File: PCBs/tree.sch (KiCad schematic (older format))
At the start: 1 part

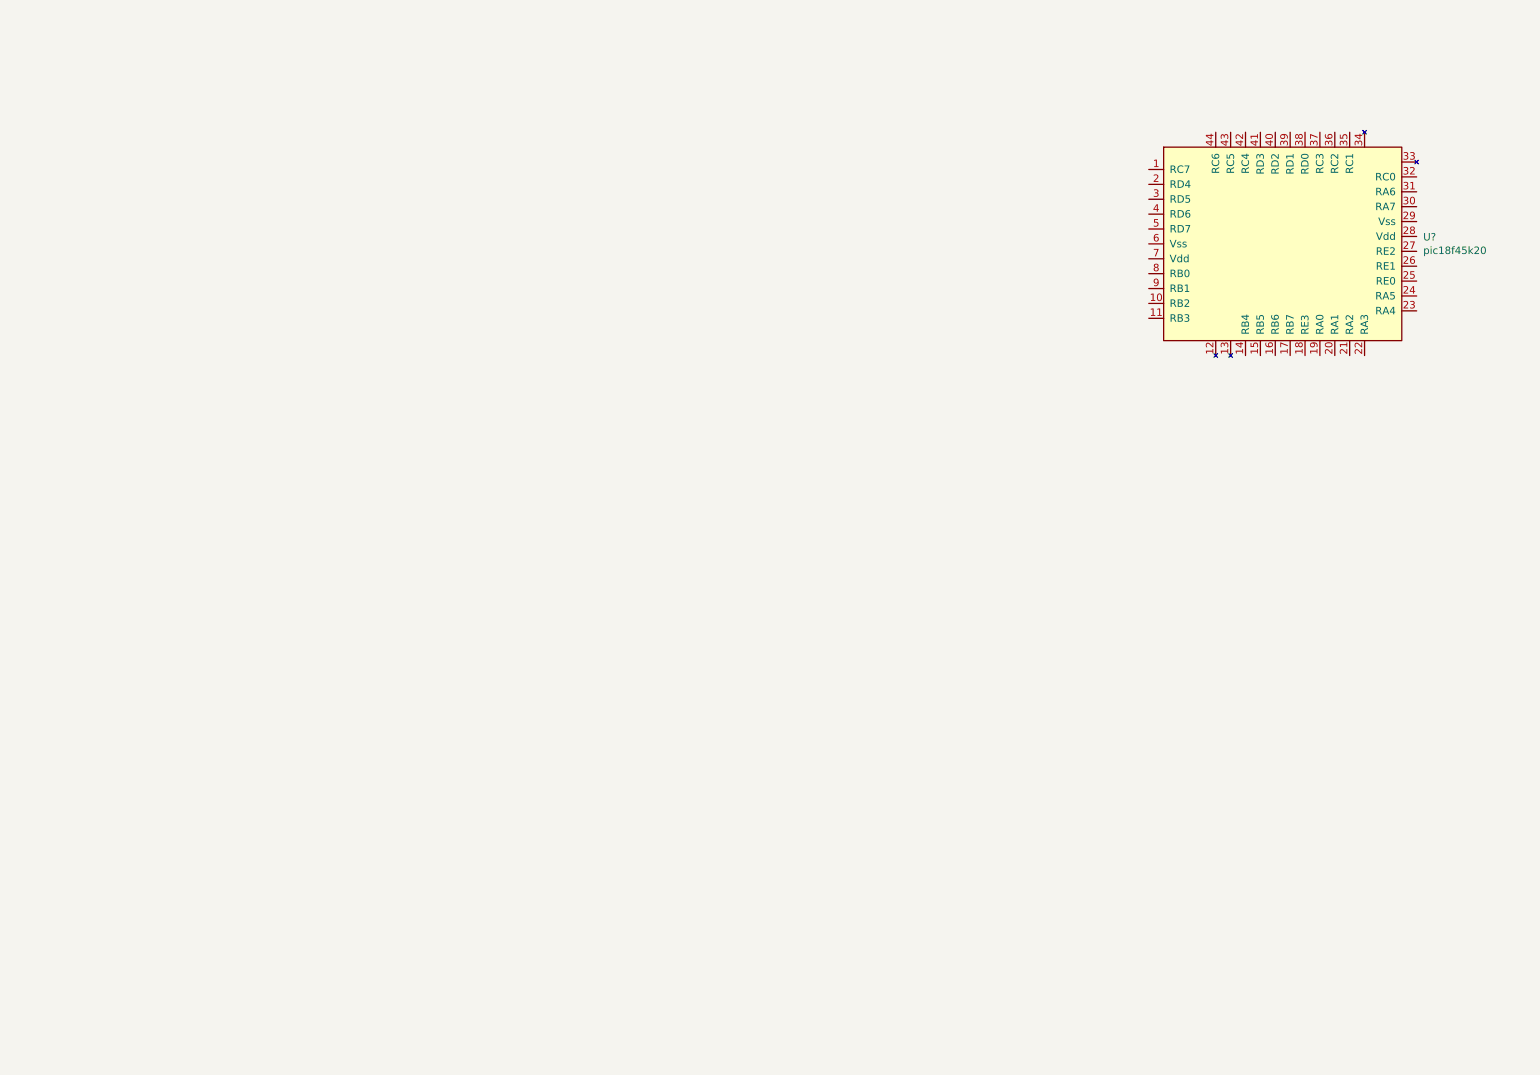
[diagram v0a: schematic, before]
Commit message: Pre-Shift Reg Schematic
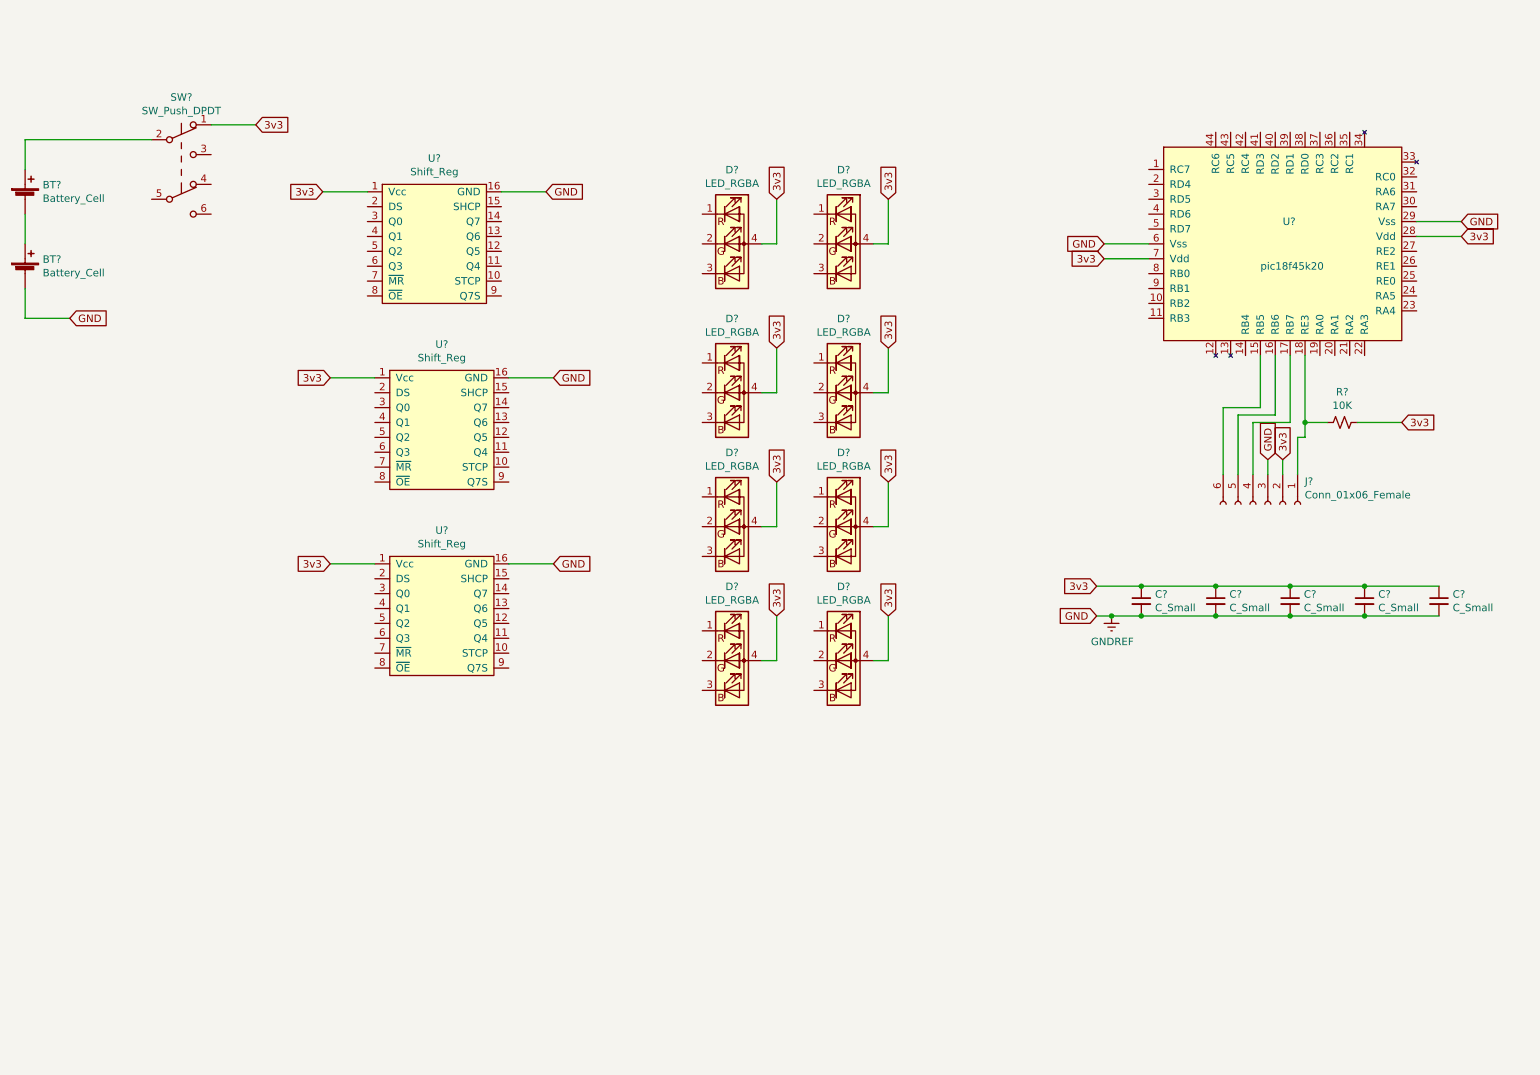
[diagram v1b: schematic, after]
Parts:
- added BT? (x2): Battery_Cell, symbol Device:Battery_Cell
- added C? (x5): C_Small, symbol Device:C_Small
- added D? (x8): LED_RGBA, symbol Device:LED_RGBA
- added J?: Conn_01x06_Female, symbol Connector:Conn_01x06_Female
- added R?: 10K, symbol Device:R_Small_US
- added SW?: SW_Push_DPDT, symbol Switch:SW_Push_DPDT
- added U? (x3): Shift_Reg, symbol NPIC6C596ADJ_shift_reg:Shift_Reg
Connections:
- net at U?.15 (RB5): now also J?.6 (Pin_6)
- net at U?.16 (RB6): now also J?.5 (Pin_5)
- net at U?.17 (RB7): now also J?.4 (Pin_4)
- net at U?.18 (RE3): now also J?.1 (Pin_1), R?.2
- net 3v3: now reaches U?.28 (Vdd)
- net 3v3: now also U?.7 (Vdd), C?.1, C?.1, C?.1, C?.1, C?.1, D?.4 (A), D?.4 (A), D?.4 (A), D?.4 (A), D?.4 (A), D?.4 (A), D?.4 (A), D?.4 (A), J?.2 (Pin_2), R?.1, SW?.1 (A), U?.1 (Vcc), U?.1 (Vcc), U?.1 (Vcc)
- net GNDREF: now reaches U?.29 (Vss)
- net GNDREF: now also U?.6 (Vss), BT?.2 (-), C?.2, C?.2, C?.2, C?.2, C?.2, J?.3 (Pin_3), U?.16 (GND), U?.16 (GND), U?.16 (GND)
- new net: BT?.1 (+), SW?.2 (B)
- new net: BT?.1 (+), BT?.2 (-)

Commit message: Finished initial revision of schematic.
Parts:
- removed D? (x4): LED_RGBA, symbol Device:LED_RGBA
- added D? (x4): LED_RGBA, symbol Device:LED_RGBA
- added D?: LED, symbol Device:LED
- added RN? (x7): R_Pack04, symbol Device:R_Pack04
- added SW?: SW_SPST, symbol Switch:SW_SPST
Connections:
- net 3v3: now also D?.4 (A), D?.4 (A), D?.4 (A), D?.4 (A), SW?.1 (A)
- net GNDREF: now also D?.1 (K), RN?.8 (R1.2)
- net Storage_CLK: now reaches U?.10 (RB2)
- net Storage_CLK: now also U?.10 (STCP), U?.10 (STCP), U?.10 (STCP)
- net ~MEM_RESET~: now reaches U?.11 (RB3)
- net ~MEM_RESET~: now also U?.7 (~MR~), U?.7 (~MR~), U?.7 (~MR~)
- net ~Output_Enable~: now reaches U?.14 (RB4)
- net ~Output_Enable~: now also U?.8 (~OE~), U?.8 (~OE~), U?.8 (~OE~)
- net HB: now reaches U?.32 (RC0)
- net HB: now also RN?.4 (R4.1)
- net B1: now reaches U?.35 (RC1)
- net B1: now also U?.3 (Q0), RN?.1 (R1.1), RN?.3 (R3.1), SW?.2 (B)
- net Red_Data: now reaches U?.8 (RB0)
- net Red_Data: now also U?.2 (DS)
- net Shift_CLK: now reaches U?.9 (RB1)
- net Shift_CLK: now also U?.15 (SHCP), U?.15 (SHCP), U?.15 (SHCP)
- net R5: now reaches U?.11 (Q4)
- net R5: now also RN?.1 (R1.1)
- net R6: now reaches U?.12 (Q5)
- net R6: now also RN?.4 (R4.1)
- net R7: now reaches U?.13 (Q6)
- net R7: now also RN?.3 (R3.1)
- net R8: now reaches U?.14 (Q7)
- net R8: now also RN?.2 (R2.1)
- net R1: now reaches U?.3 (Q0)
- net R1: now also RN?.1 (R1.1)
- net R2: now reaches U?.4 (Q1)
- net R2: now also RN?.4 (R4.1)
- net R3: now reaches U?.5 (Q2)
- net R3: now also RN?.3 (R3.1)
- net R4: now reaches U?.6 (Q3)
- net R4: now also RN?.2 (R2.1)
- net Green_Data: now reaches U?.9 (Q7S)
- net Green_Data: now also U?.2 (DS)
- net at D?.1 (RK): now also RN?.5 (R4.2)
- net at D?.2 (GK): now also RN?.8 (R1.2)
- net at D?.3 (BK): now also RN?.7 (R2.2)
- net at D?.1 (RK): now also RN?.8 (R1.2)
- net at D?.2 (GK): now also RN?.7 (R2.2)
- net at D?.3 (BK): now also RN?.6 (R3.2)
- net at D?.1 (RK): now also RN?.6 (R3.2)
- net at D?.2 (GK): now also RN?.5 (R4.2)
- net at D?.3 (BK): now also RN?.8 (R1.2)
- net at D?.1 (RK): now also RN?.7 (R2.2)
- net at D?.2 (GK): now also RN?.6 (R3.2)
- net at D?.3 (BK): now also RN?.5 (R4.2)
- net G5: now reaches U?.11 (Q4)
- net G5: now also RN?.2 (R2.1)
- net G6: now reaches U?.12 (Q5)
- net G6: now also RN?.1 (R1.1)
- net G7: now reaches U?.13 (Q6)
- net G7: now also RN?.4 (R4.1)
- net G8: now reaches U?.14 (Q7)
- net G8: now also RN?.3 (R3.1)
- net G1: now reaches U?.3 (Q0)
- net G1: now also RN?.2 (R2.1)
- net G2: now reaches U?.4 (Q1)
- net G2: now also RN?.1 (R1.1)
- net G3: now reaches U?.5 (Q2)
- net G3: now also RN?.4 (R4.1)
- net G4: now reaches U?.6 (Q3)
- net G4: now also RN?.3 (R3.1)
- net Blue_Data: now reaches U?.9 (Q7S)
- net Blue_Data: now also U?.2 (DS)
- net B5: now reaches U?.11 (Q4)
- net B5: now also RN?.3 (R3.1)
- net B6: now reaches U?.12 (Q5)
- net B6: now also RN?.2 (R2.1)
- net B7: now reaches U?.13 (Q6)
- net B7: now also RN?.1 (R1.1)
- net B8: now reaches U?.14 (Q7)
- net B8: now also RN?.4 (R4.1)
- net B2: now reaches U?.4 (Q1)
- net B2: now also RN?.2 (R2.1)
- net B3: now reaches U?.5 (Q2)
- net B3: now also RN?.1 (R1.1)
- net B4: now reaches U?.6 (Q3)
- net B4: now also RN?.4 (R4.1)
- new net: D?.1 (RK), RN?.5 (R4.2)
- new net: D?.2 (GK), RN?.8 (R1.2)
- new net: D?.3 (BK), RN?.7 (R2.2)
- new net: D?.1 (RK), RN?.8 (R1.2)
- new net: D?.2 (GK), RN?.7 (R2.2)
- new net: D?.3 (BK), RN?.6 (R3.2)
- new net: D?.1 (RK), RN?.6 (R3.2)
- new net: D?.2 (GK), RN?.5 (R4.2)
- new net: D?.3 (BK), RN?.8 (R1.2)
- new net: D?.1 (RK), RN?.7 (R2.2)
- new net: D?.2 (GK), RN?.6 (R3.2)
- new net: D?.3 (BK), RN?.5 (R4.2)
- new net: D?.2 (A), RN?.5 (R4.2)
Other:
- moved on the sheet: D?, U?

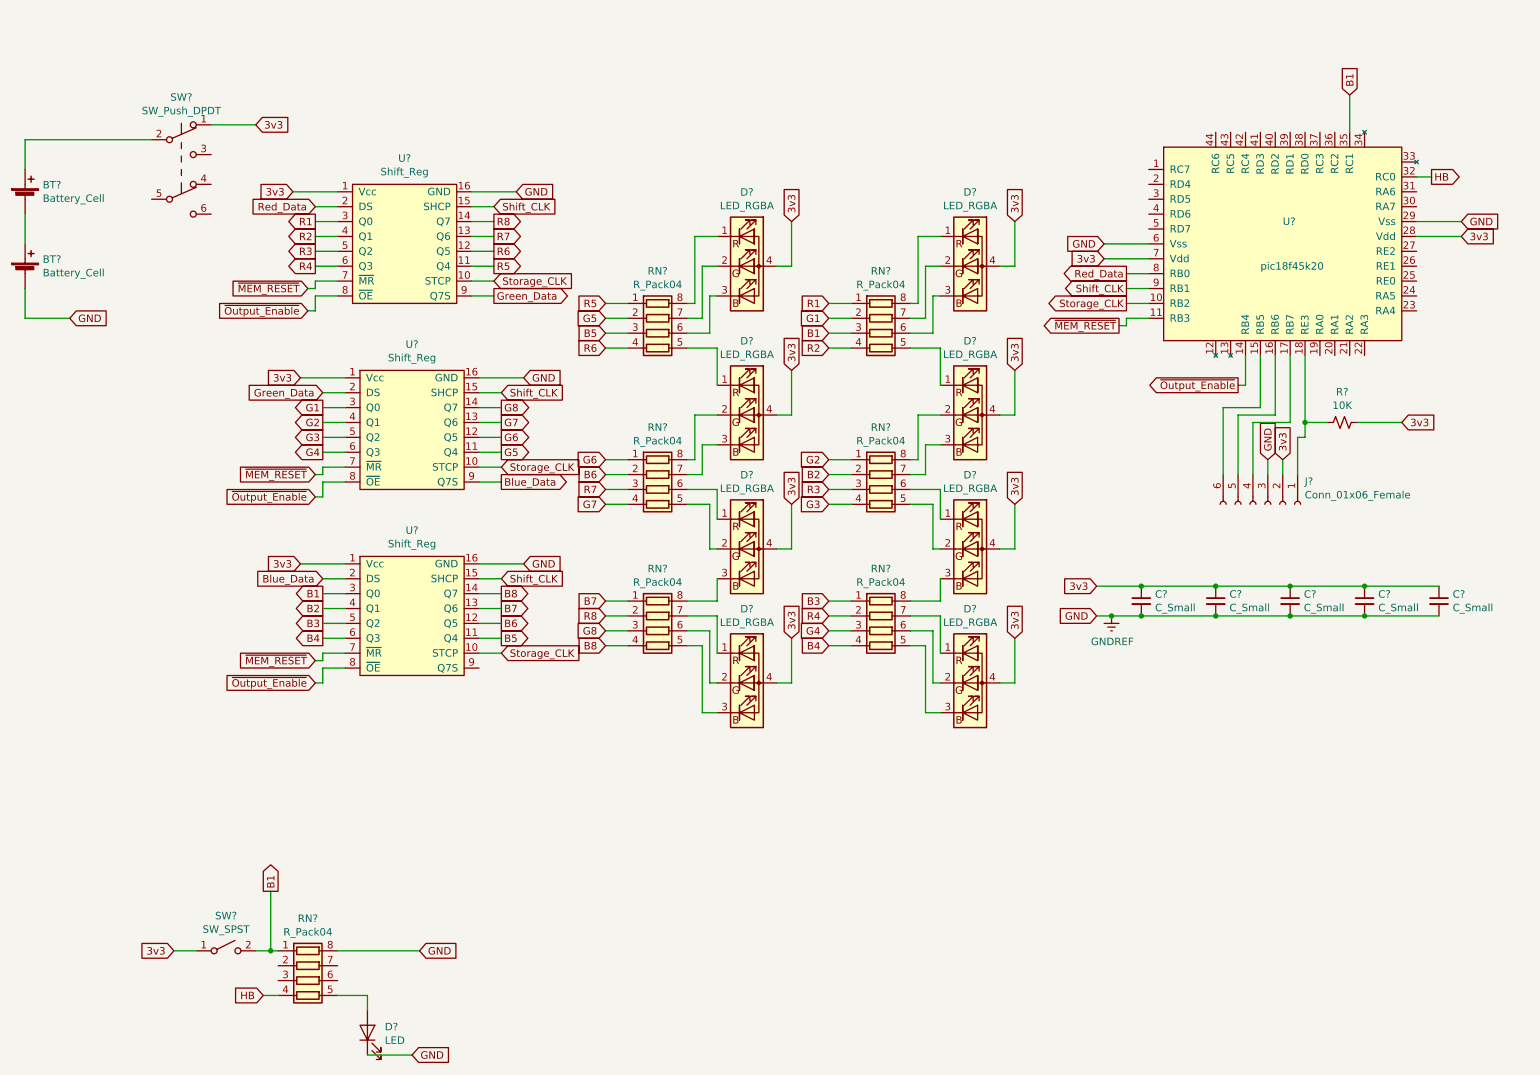
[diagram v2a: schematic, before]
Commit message: Correct several footprint issues. Addressed symbol glitch. Some routing handled.
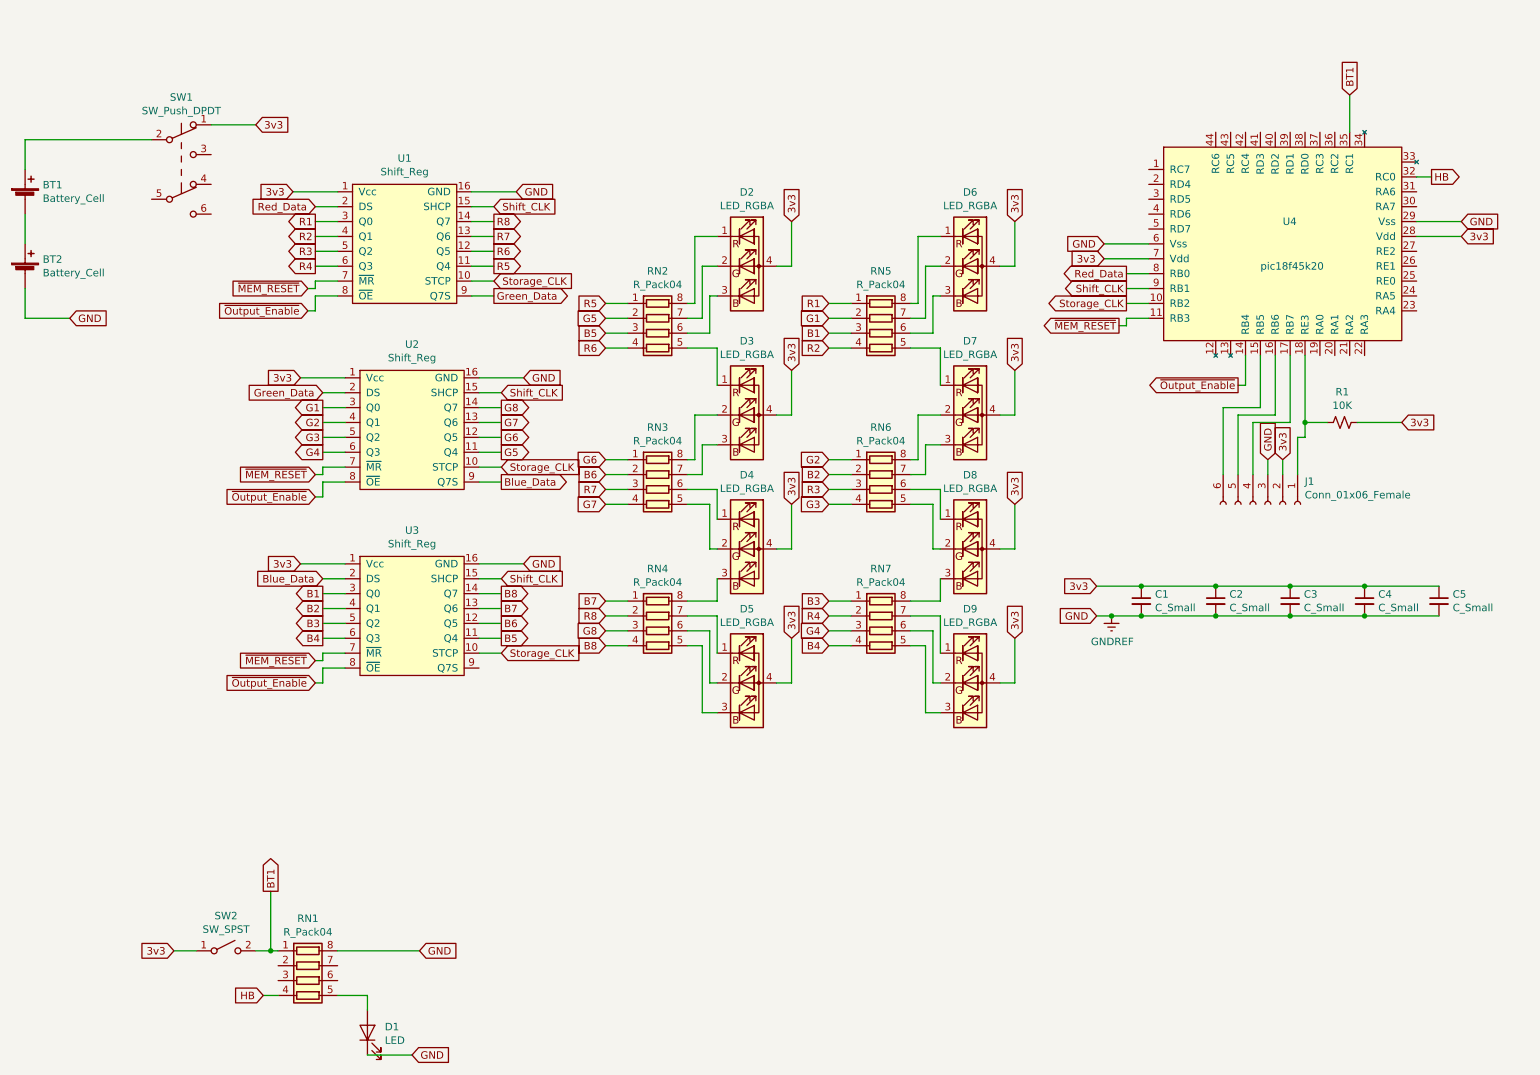
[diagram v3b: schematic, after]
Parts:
- BT1, BT2: renamed from BT?; footprint (none) -> Battery:BatteryHolder_Keystone_2460_1xAA
- C1, C2, C3, C4, C5: renamed from C?; footprint (none) -> Capacitor_SMD:C_0805_2012Metric_Pad1.15x1.40mm_HandSolder
- D1: renamed from D?; footprint (none) -> LED_SMD:LED_0603_1608Metric_Pad1.05x0.95mm_HandSolder
- D2, D3, D4, D5, D6, D7, D8, D9: renamed from D?; footprint (none) -> LED_SMD:LED_Cree-PLCC4_2x2mm_CW
- J1: renamed from J?; footprint (none) -> Connector_PinHeader_2.54mm:PinHeader_1x06_P2.54mm_Vertical
- R1: renamed from R?; footprint (none) -> Resistor_SMD:R_0805_2012Metric
- RN1, RN2, RN3, RN4, RN5, RN6, RN7: renamed from RN?; footprint (none) -> Resistor_SMD:R_Array_Convex_4x0603
- SW1: renamed from SW?; footprint (none) -> JS202011SCQN:JS202011SCQN
- SW2: renamed from SW?; footprint (none) -> LL3301FF065QJ_pushbutton:LL3301FF065QJ
- U1, U2, U3: renamed from U?; footprint (none) -> Package_SO:TSSOP-16_4.4x5mm_P0.65mm
- U4: renamed from U?; footprint (none) -> Package_QFP:LQFP-44_10x10mm_P0.8mm
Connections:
- net B1: no longer RN1.1 (R1.1), SW2.2 (B), U4.35 (RC1)
- new net BT1: RN1.1 (R1.1), SW2.2 (B), U4.35 (RC1)
